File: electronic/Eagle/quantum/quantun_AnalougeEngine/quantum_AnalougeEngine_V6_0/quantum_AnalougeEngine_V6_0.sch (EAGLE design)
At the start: 279 parts, among them IC1 OP275, IC10 STM32F767ZIT6, IC11 PGA2320IDW, IC12 ESDA6V1BC6, IC13 USBLC6-4SC6, IC16 OP275, IC17 AD7606BSTZ-6, IC2 DAC084S085CIMM_NOPB, IC4 OP275, IC6 LAN8742A-CZ-TR, IC8 OP275, IC9 NE5532, J1 GWLEX-SMT-S988G_Y, K1 Relay, K2 Relay, K3 Relay, K4 Relay, K5 Relay, K6 Relay, K7 Relay, K8 Relay, T1 H1102NL, U1 78_SMD, U12 ULN2003, U4 THAT1240, U6 THAT1240, U7 THAT1240, U8 THAT1240, Y1 NX3215SA-32.768K-STD-MUA-8, Y2 NX3225GD-8MHZ-STD-CRA-3, Y3 ABLS2-25.000MHZ-D4YF-T

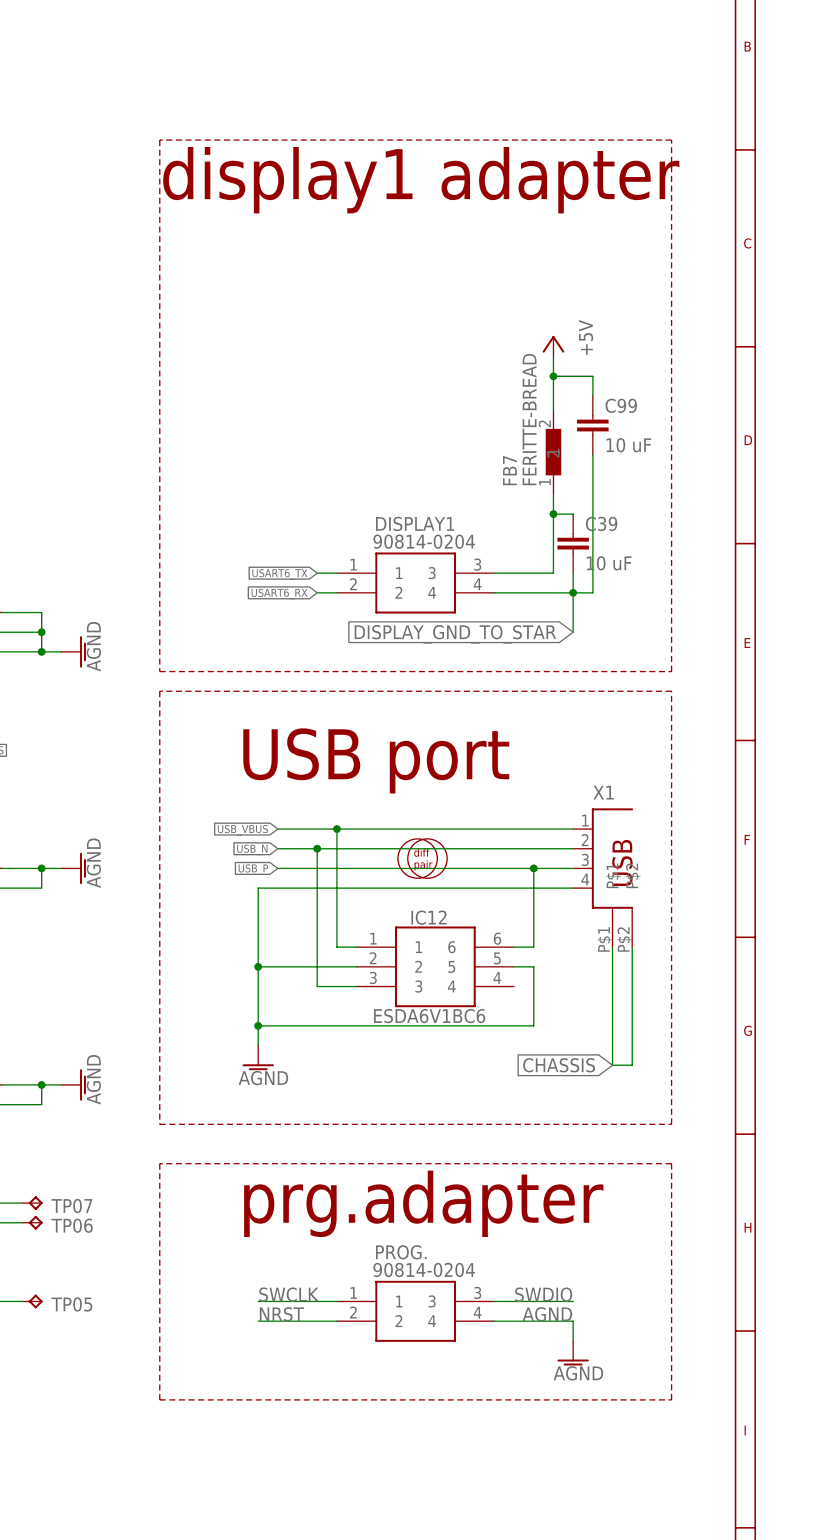
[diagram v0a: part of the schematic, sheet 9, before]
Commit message: OpenBLT TCP-IP -- UART Bridge
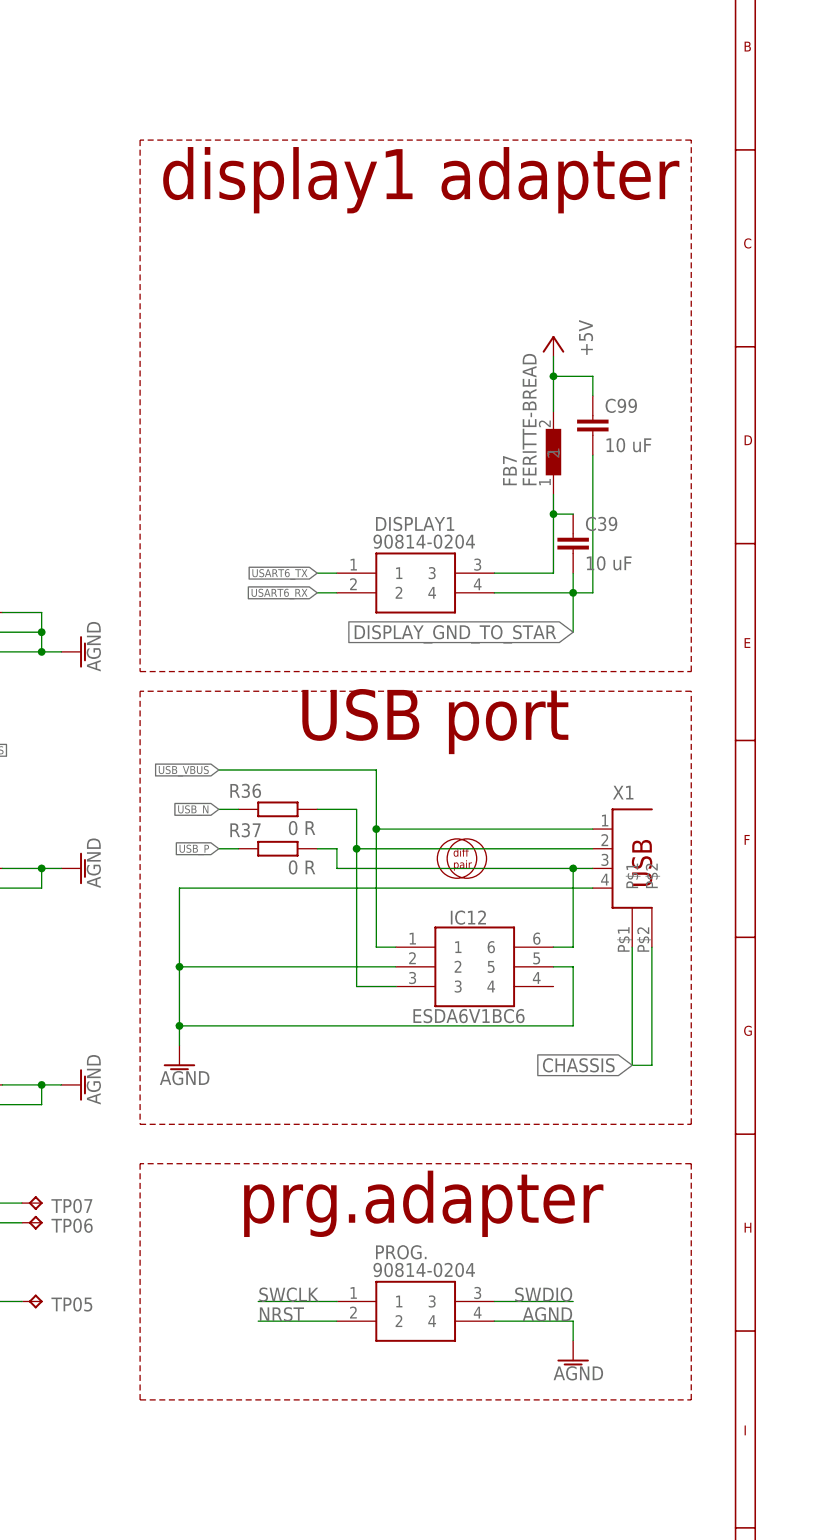
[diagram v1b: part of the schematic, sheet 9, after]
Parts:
- added R36, R37: 0 R, passive components:RESISTOR_0603
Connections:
- new net USB_N_AFTER: IC12.3, R36.2, X1.2
- new net USB_P_AFTER: IC12.6, R37.2, X1.3
- net USB_N: now also R36.1; no longer IC12.3, X1.2
- net USB_P: now also R37.1; no longer IC12.6, X1.3
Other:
- moved on the sheet: IC12, X1
